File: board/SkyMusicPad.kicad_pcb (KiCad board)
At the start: 2 copper layers, 117.5 x 62.5 mm, 36 parts, among them SW1 Cherry, SW10 Cherry, SW11 Cherry, SW12 Cherry, SW13 Cherry, SW14 Cherry, SW15 Cherry, SW16 RotaryEncoder_Switch, SW2 Cherry, SW3 Cherry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

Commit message: Hardware changes, 3D regen
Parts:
- added REF**: OSHW-Logo2_7.3x6mm_Copper, Symbol:OSHW-Logo2_7.3x6mm_Copper, F.Cu at (153.5, 35.0)
- moved D11 21.3 mm to (116.2, 55.0)
- moved D5 21.3 mm to (81.2, 55.0)
- moved D10 21.3 mm to (116.2, 37.5)
- moved D4 21.3 mm to (81.2, 37.5)
- moved D2 21.3 mm to (67.2, 48.0)
- moved D14 21.2 mm to (133.8, 55.0)
- moved D8 21.2 mm to (98.8, 55.0)
- moved D1 21.2 mm to (63.8, 37.5)
- moved D13 21.2 mm to (133.8, 37.5)
- moved D7 21.2 mm to (98.8, 37.5)
- moved SW2 21.0 mm to (72.5, 55.0)
- moved SW11 21.0 mm to (125.0, 55.0)
- moved SW14 21.0 mm to (142.5, 55.0)
- moved SW5 21.0 mm to (90.0, 55.0)
- moved SW8 21.0 mm to (107.5, 55.0)
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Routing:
- net Row0: track 78.6 -> 89.3 mm
- net Row1: track 85.9 -> 94.2 mm
- net Rot_SW: track 19.8 -> 24.6 mm
- net Row2: track 106.5 -> 109.3 mm
- net Net-(D7-A): track 7.48 -> 5.09 mm
- net Net-(D4-A): track 7.58 -> 5.19 mm
- net Net-(D5-A): track 7.48 -> 5.17 mm
- net Net-(D10-A): track 7.47 -> 5.19 mm
- net Net-(D1-A): track 7.48 -> 5.32 mm
- net Net-(D13-A): track 7.25 -> 5.09 mm
- net Net-(D11-A): track 7.36 -> 5.30 mm
- net Net-(D14-A): track 7.32 -> 5.30 mm
- net Net-(D8-A): track 7.32 -> 5.30 mm
- net Col0: track 50.2 -> 51.7 mm
- net Net-(D9-A): track 4.58 -> 5.62 mm
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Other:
- outline, holes or cut-outs redrawn

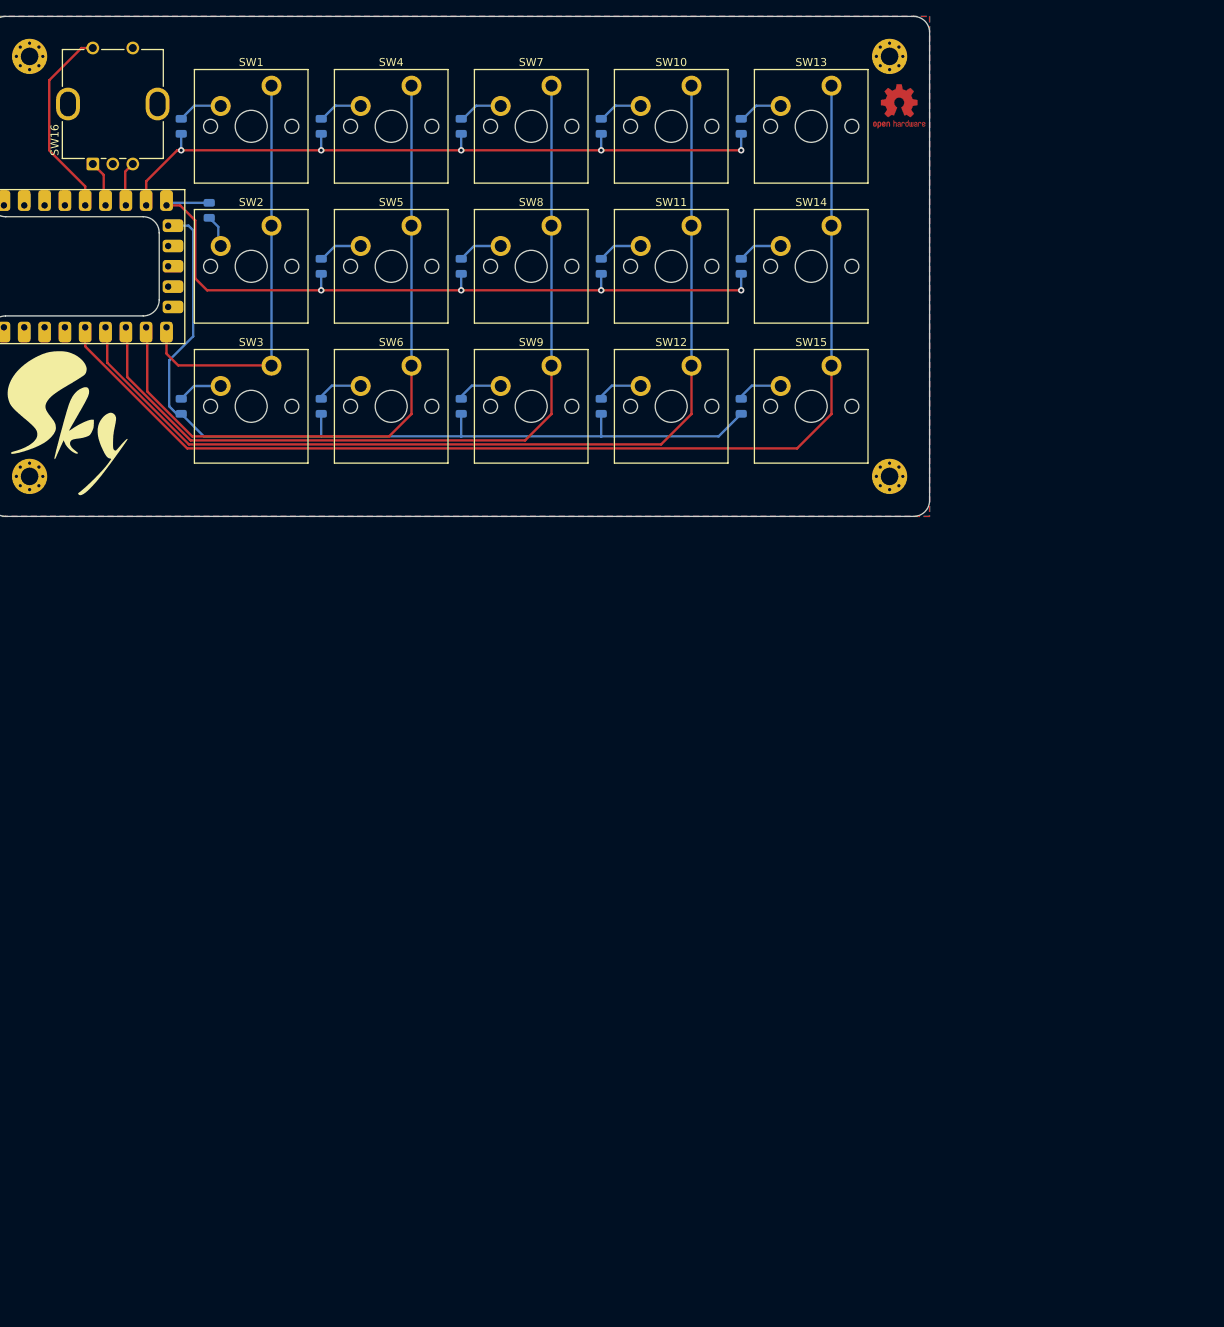
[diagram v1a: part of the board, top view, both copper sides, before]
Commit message: Adjusting design for larger board
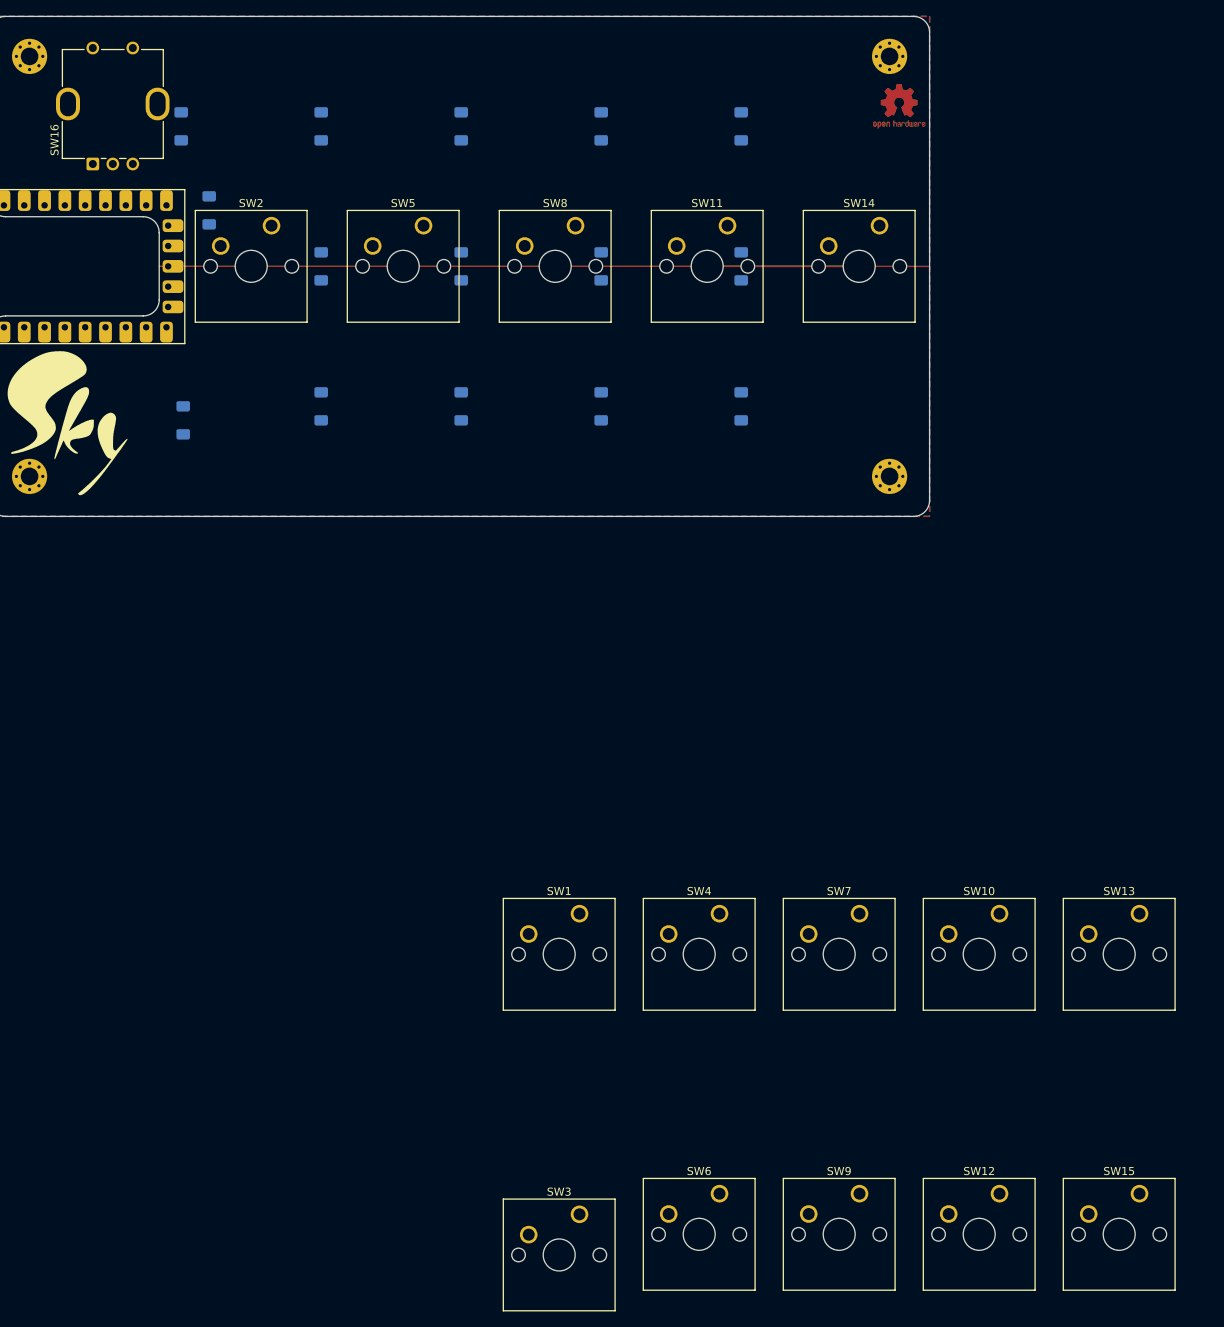
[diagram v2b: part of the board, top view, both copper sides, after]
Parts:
- D1, D10, D11, D12, D13, D14, D15, D2, D3, D4, D5, D6, D7, D8, D9: footprint Diode_SMD:D_0805_2012Metric -> Diode_SMD:D_MiniMELF
- SW1, SW10, SW11, SW12, SW13, SW14, SW15, SW2, SW3, SW4, SW5, SW6, SW7, SW8, SW9: footprint PCM_Switch_Keyboard_Cherry_MX:SW_Cherry_MX_PCB -> SkyMusic:SW_Cherry_MX_1.00u_PCB
- moved SW3 112.9 mm to (111.0, 178.6)
- moved SW1 110.4 mm to (111.0, 141.0)
- moved SW10 110.4 mm to (163.5, 141.0)
- moved SW12 110.4 mm to (163.5, 176.0)
- moved SW13 110.4 mm to (181.0, 141.0)
- moved SW15 110.4 mm to (181.0, 176.0)
- moved SW4 110.4 mm to (128.5, 141.0)
- moved SW6 110.4 mm to (128.5, 176.0)
- moved SW7 110.4 mm to (146.0, 141.0)
- moved SW9 110.4 mm to (146.0, 176.0)
- moved SW14 6.00 mm to (148.5, 55.0)
- moved SW11 4.50 mm to (129.5, 55.0)
- moved SW8 3.00 mm to (110.5, 55.0)
- moved D3 1.77 mm to (64.0, 74.2)
- moved SW5 1.50 mm to (91.5, 55.0)
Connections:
- SW1 pad 1: Net-(D1-A) -> Col0
- SW1 pad 2: Col0 -> Net-(D1-A)
- SW10 pad 1: Net-(D10-A) -> Col3
- SW10 pad 2: Col3 -> Net-(D10-A)
- SW11 pad 1: Net-(D11-A) -> Col3
- SW11 pad 2: Col3 -> Net-(D11-A)
- SW12 pad 1: Net-(D12-A) -> Col3
- SW12 pad 2: Col3 -> Net-(D12-A)
- SW13 pad 1: Net-(D13-A) -> Col4
- SW13 pad 2: Col4 -> Net-(D13-A)
- SW14 pad 1: Net-(D14-A) -> Col4
- SW14 pad 2: Col4 -> Net-(D14-A)
- SW15 pad 1: Net-(D15-A) -> Col4
- SW15 pad 2: Col4 -> Net-(D15-A)
- SW2 pad 1: Net-(D2-A) -> Col0
- SW2 pad 2: Col0 -> Net-(D2-A)
- SW3 pad 1: Net-(D3-A) -> Col0
- SW3 pad 2: Col0 -> Net-(D3-A)
- SW4 pad 1: Net-(D4-A) -> Col1
- SW4 pad 2: Col1 -> Net-(D4-A)
- SW5 pad 1: Net-(D5-A) -> Col1
- SW5 pad 2: Col1 -> Net-(D5-A)
- SW6 pad 1: Net-(D6-A) -> Col1
- SW6 pad 2: Col1 -> Net-(D6-A)
- SW7 pad 1: Net-(D7-A) -> Col2
- SW7 pad 2: Col2 -> Net-(D7-A)
- SW8 pad 1: Net-(D8-A) -> Col2
- SW8 pad 2: Col2 -> Net-(D8-A)
- SW9 pad 1: Net-(D9-A) -> Col2
- SW9 pad 2: Col2 -> Net-(D9-A)
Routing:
- net Col4: track 143.8 -> 0.00 mm
- net Col3: track 124.4 -> 0.00 mm
- net Row2: track 109.3 -> 0.00 mm
- net Col2: track 105.0 -> 0.00 mm
- net Row1: track 94.2 -> 0.00 mm, vias 4 -> 0
- net Row0: track 89.3 -> 0.00 mm, vias 5 -> 0
- net Col1: track 85.6 -> 0.00 mm
- net Col0: track 51.7 -> 0.00 mm
- net Rot_SW: track 24.6 -> 0.00 mm
- net Rot_A: track 5.83 -> 0.00 mm
- net Net-(D9-A): track 5.62 -> 0.00 mm
- net Net-(D6-A): track 5.62 -> 0.00 mm
- net Net-(D12-A): track 5.62 -> 0.00 mm
- net Net-(D15-A): track 5.62 -> 0.00 mm
- net Net-(D3-A): track 5.60 -> 0.00 mm
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
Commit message: Board and code update
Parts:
- moved SW1 111.0 mm to (75.0, 36.0)
- moved SW3 110.6 mm to (75.0, 74.0)
- moved SW4 110.5 mm to (94.0, 36.0)
- moved SW7 110.1 mm to (113.0, 36.0)
- moved SW10 109.6 mm to (132.0, 36.0)
- moved SW13 109.2 mm to (151.0, 36.0)
- moved SW6 107.7 mm to (94.0, 74.0)
- moved SW9 107.2 mm to (113.0, 74.0)
- moved SW12 106.8 mm to (132.0, 74.0)
- moved SW15 106.3 mm to (151.0, 74.0)
- moved D15 13.4 mm to (146.0, 78.0)
- moved D14 12.9 mm to (146.0, 59.0)
- moved H2 12.7 mm to (165.0, 28.8)
- moved H4 12.7 mm to (165.0, 81.3)
- moved D13 12.5 mm to (146.0, 40.0)
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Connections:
- RZ1 pad 10: unconnected-(RZ1-GP10-Pad10) -> Row2
- RZ1 pad 7: Row0 -> unconnected-(RZ1-GP7-Pad7)
- RZ1 pad 8: Row1 -> Row0
- RZ1 pad 9: Row2 -> Row1
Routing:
- net Col4: track 0.00 -> 169.0 mm
- net Col3: track 0.00 -> 148.1 mm
- net Col2: track 0.00 -> 127.2 mm
- net Row2: track 0.00 -> 121.4 mm, vias 0 -> 5
- net Col1: track 0.00 -> 106.4 mm
- net Row1: track 0.00 -> 105.8 mm, vias 0 -> 5
- net Row0: track 0.00 -> 98.1 mm, vias 0 -> 5
- net Col0: track 0.00 -> 85.6 mm
- net Rot_SW: track 0.00 -> 25.3 mm
- net Rot_A: track 0.00 -> 5.89 mm
- net Rot_B: track 0.00 -> 5.89 mm
- net Net-(D9-A): track 0.00 -> 5.28 mm
- net Net-(D6-A): track 0.00 -> 5.28 mm
- net Net-(D3-A): track 0.00 -> 5.28 mm
- net Net-(D15-A): track 0.00 -> 5.28 mm
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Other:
- board size 117.5 x 62.5 mm -> 130 x 62.5 mm

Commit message: More misc updates
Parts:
- moved H4 0.25 mm to (164.8, 81.2)
- moved H2 0.25 mm to (164.8, 28.8)
- moved H3 0.05 mm to (44.8, 81.2)
- moved H1 0.05 mm to (44.8, 28.8)
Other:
- board text added: "Designed by @voxeltek and @citacritta Assembled by hand in Australia This is an unnofficial community project"
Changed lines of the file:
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@@
 		(attr smd)
 		(fp_line
-			(start 9.59 -11)
-			(end -9.66 -11)
-			(stroke
-				(width 0.12)
-				(type solid)
-			)
-			(layer "F.SilkS")
-		)
-		(fp_line
 			(start -9.66 -11)
 			(end -9.66 13.2)
@@
 	(footprint "MountingHole:MountingHole_2.2mm_M2_Pad_Via"
 		(layer "F.Cu")
-		(at 44.8 81.26)
+		(at 44.75 81.25)
 		(descr "Mounting Hole 2.2mm, M2")
 		(tags "mounting hole 2.2mm m2")
@@
 	(footprint "MountingHole:MountingHole_2.2mm_M2_Pad_Via"
 		(layer "F.Cu")
-		(at 165 28.76)
+		(at 164.75 28.75)
 		(descr "Mounting Hole 2.2mm, M2")
 		(tags "mounting hole 2.2mm m2")
@@
 	(footprint "MountingHole:MountingHole_2.2mm_M2_Pad_Via"
 		(layer "F.Cu")
-		(at 44.8 28.76)
+		(at 44.75 28.75)
 		(descr "Mounting Hole 2.2mm, M2")
 		(tags "mounting hole 2.2mm m2")
@@
 	(footprint "MountingHole:MountingHole_2.2mm_M2_Pad_Via"
 		(layer "F.Cu")
-		(at 165 81.26)
+		(at 164.75 81.25)
 		(descr "Mounting Hole 2.2mm, M2")
 		(tags "mounting hole 2.2mm m2")
@@
 		(layer "Edge.Cuts")
 	)
+	(gr_text "Designed by @voxeltek and @citacritta\nAssembled by hand in Australia\n\n\n\n\n\n\nThis is an unnofficial community project"
+		(at 104.75 54.75 0)
+		(layer "B.SilkS")
+		(effects
+			(font
+				(size 1.5 1.5)
+				(thickness 0.3)
+				(bold yes)
+			)
+			(justify mirror)
+		)
+	)
 	(segment
